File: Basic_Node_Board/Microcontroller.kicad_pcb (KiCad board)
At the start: 4 copper layers, 100 x 100 mm, 31 parts, among them J1 Conn_01x02, J4 Conn_01x02_Pin, U2 ESP32-DEVKIT-C, U3 TPS54560BQDDARQ1, U6 TJA1050T/CM,118

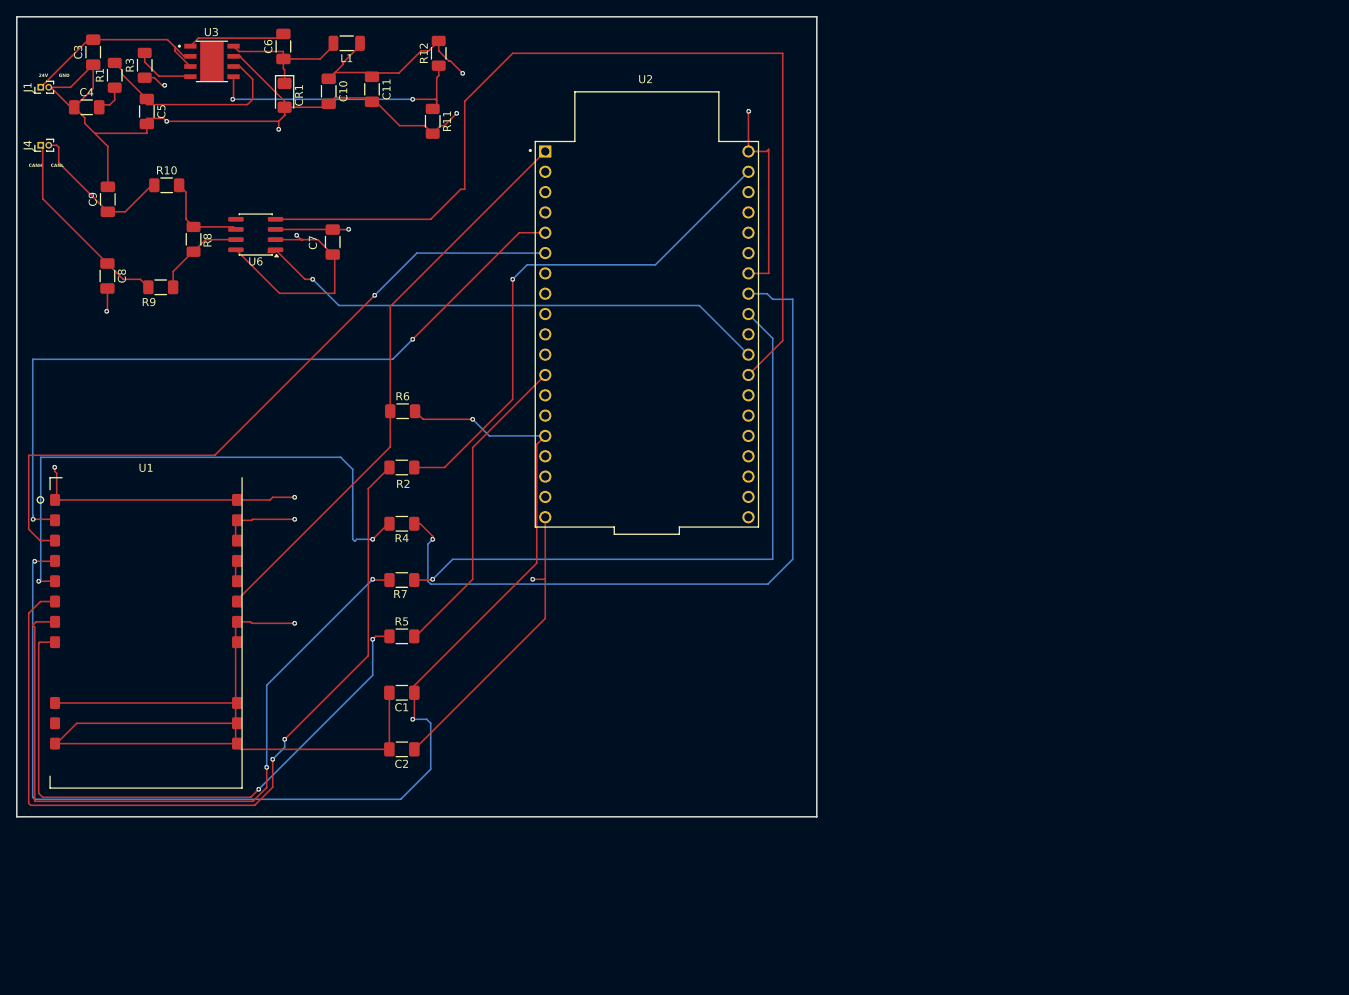
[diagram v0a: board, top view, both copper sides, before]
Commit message: Julia's IMU PCB (Incomplete)
PCB with 24-5V buck converter, CAN Transceiver, ESP, thermal resistor connector, humidity sensor, SDIO breakout board, Adafruit ICM breakout board.

*******INCOMPLETE DESIGN*******
Capacitances for the buck converter and J1 and J4 connectors are INCORRECT, need to be adjusted before ordering.
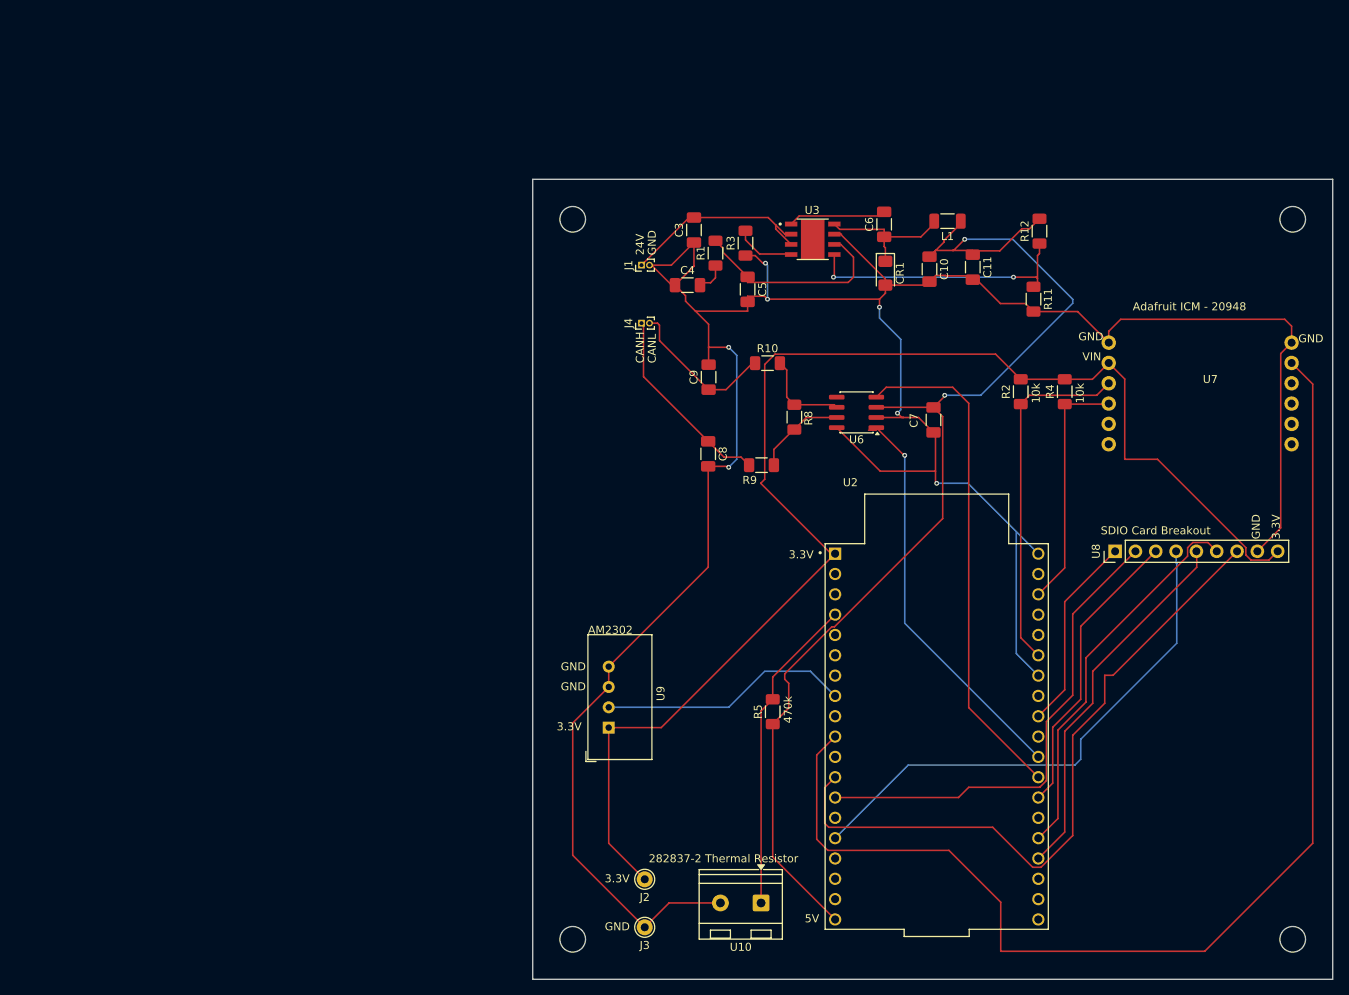
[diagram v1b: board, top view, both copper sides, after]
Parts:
- removed C1: 100nF, Capacitor_SMD:C_1206_3216Metric_Pad1.33x1.80mm_HandSolder
- removed C2: 100uF, Capacitor_SMD:C_1206_3216Metric_Pad1.33x1.80mm_HandSolder
- removed R6: 10k, Resistor_SMD:R_1206_3216Metric_Pad1.30x1.75mm_HandSolder
- removed R7: 100, Resistor_SMD:R_1206_3216Metric_Pad1.30x1.75mm_HandSolder
- removed U1: ~, PROVE-footprints:E22P-915M30S_revised
- added J2: Conn_01x19_Socket, Connector_Pin:Pin_D1.0mm_L10.0mm, F.Cu at (114.0, 132.5)
- added J3: Conn_01x19_Socket, Connector_Pin:Pin_D1.0mm_L10.0mm, F.Cu at (114.0, 138.5)
- added REF**: MountingHole_3.2mm_M3, MountingHole:MountingHole_3.2mm_M3, F.Cu at (105.0, 140.0)
- added REF**: MountingHole_3.2mm_M3, MountingHole:MountingHole_3.2mm_M3, F.Cu at (195.0, 50.0)
- added REF**: MountingHole_3.2mm_M3, MountingHole:MountingHole_3.2mm_M3, F.Cu at (195.0, 140.0)
- added REF**: MountingHole_3.2mm_M3, MountingHole:MountingHole_3.2mm_M3, F.Cu at (105.0, 50.0)
- added U10: Thermal Resistor, TerminalBlock_RND:TerminalBlock_RND_205-00232_1x02_P5.08mm_Horizontal, F.Cu at (128.5, 135.5)
- added U7: Adafruit ICM-20948, Julias_IMU_Footprint_Library:Adafruit_ICM20948_2x6_Module, F.Cu at (184.7, 73.0)
- added U8: SDIO Card Breakout Board, Connector_PinHeader_2.54mm:PinHeader_1x09_P2.54mm_Vertical, F.Cu at (172.8, 91.5)
- added U9: AM2302, Sensor:ASAIR_AM2302_P2.54mm_Vertical, F.Cu at (109.5, 113.5)
- R2, R4: value 100 -> 10k
- R5: value 100 -> 470k
- U2: footprint PROVE-footprints:MODULE_ESP32-DEVKITC -> PROVE:MODULE_ESP32-DEVKITC
- moved R4 84.5 mm to (166.5, 71.5), turned to 90 degrees
- moved R8 78.3 mm to (132.7, 74.7)
- moved C3 78.3 mm to (120.2, 51.3)
- moved C4 78.3 mm to (119.3, 58.2)
- moved C8 78.3 mm to (121.9, 79.3)
- moved J1 78.3 mm to (113.6, 55.7)
- moved J4 78.3 mm to (113.6, 63.0)
- moved R1 78.3 mm to (122.8, 54.2)
- moved R3 78.3 mm to (126.6, 53.0)
- moved U3 78.3 mm to (135.0, 52.5)
- moved C10 78.3 mm to (149.6, 56.2)
- moved C11 78.3 mm to (155.0, 56.0)
- moved C5 78.3 mm to (126.9, 58.8)
- moved C6 78.3 mm to (143.9, 50.6)
- moved C7 78.3 mm to (150.1, 75.1)
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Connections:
- R2 pad 1: Net-(J3-Pin_2) -> Net-(J3-Pin_6)
- R2 pad 2: Net-(U1-MOSI) -> Net-(J2-Pin_1)
- R4 pad 1: Net-(J3-Pin_8) -> Net-(J3-Pin_3)
- R4 pad 2: Net-(U1-MISO) -> Net-(J2-Pin_1)
- R5 pad 1: Net-(U1-NSS) -> 5.3V OUT
- R5 pad 2: Net-(J2-Pin_12) -> Net-(J2-Pin_4)
- U2 pad 14: Net-(J2-Pin_14) -> unconnected-(J2-Pin_14-Pad14)
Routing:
- net Net-(J2-Pin_10): track 0.00 -> 151.9 mm
- net GND: track 468.5 -> 341.7 mm, vias 10 -> 7
- net Net-(U1-MOSI): track 105.2 -> 0.00 mm, vias 2 -> 0
- net Net-(J2-Pin_1): track 72.6 -> 170.0 mm
- net Net-(J3-Pin_8): track 94.2 -> 0.00 mm, vias 1 -> 0
- net Net-(J2-Pin_5): track 93.6 -> 0.00 mm, vias 2 -> 0
- net Net-(U1-SCK): track 88.9 -> 0.00 mm, vias 2 -> 0
- net Net-(J2-Pin_6): track 88.3 -> 0.00 mm, vias 1 -> 0
- net Net-(J2-Pin_15): track 152.2 -> 65.8 mm, vias 3 -> 0
- net Net-(U1-NSS): track 76.5 -> 0.00 mm, vias 2 -> 0
- net Net-(U1-MISO): track 71.9 -> 0.00 mm, vias 2 -> 0
- net Net-(J3-Pin_2): track 65.9 -> 0.00 mm, vias 1 -> 0
- net Net-(J2-Pin_13): track 0.00 -> 60.6 mm
- net Net-(J3-Pin_12): track 120.4 -> 63.2 mm
- net Net-(J3-Pin_9): track 77.8 -> 24.6 mm, vias 1 -> 0
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- removed copper zone on In1.Cu, net 5.3V OUT
- removed copper zone on In2.Cu, net GND
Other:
- copper layers 4 -> 2
- board text added: "10k"
- board text added: "282837-2 Thermal Resistor"
- board text added: "3.3V"
- board text added: "470k"
- board text added: "5V"
- board text added: "AM2302"
- board text added: "Adafruit ICM - 20948"
- board text added: "SDIO Card Breakout"
